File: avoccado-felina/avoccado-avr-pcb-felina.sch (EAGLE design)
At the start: 68 parts, among them Q1 16MHz, Q2 FET, U1 MPU-6000QFN-24, U2 MCP73831

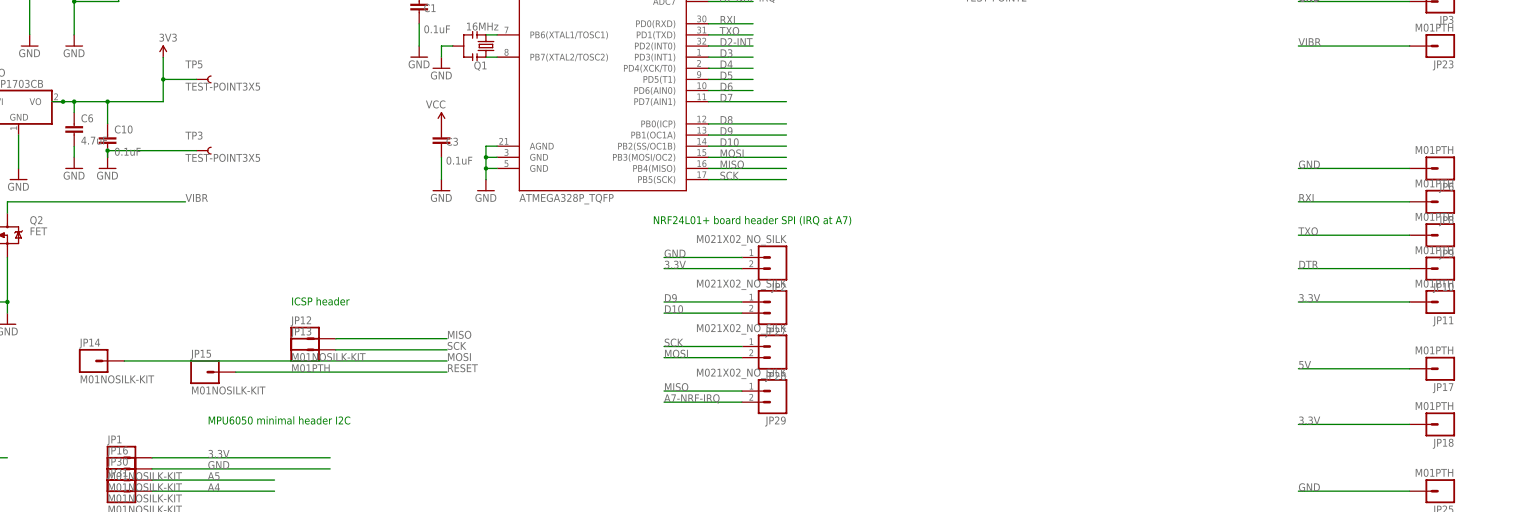
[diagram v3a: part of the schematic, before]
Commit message: Vcc and GND routed at bottom
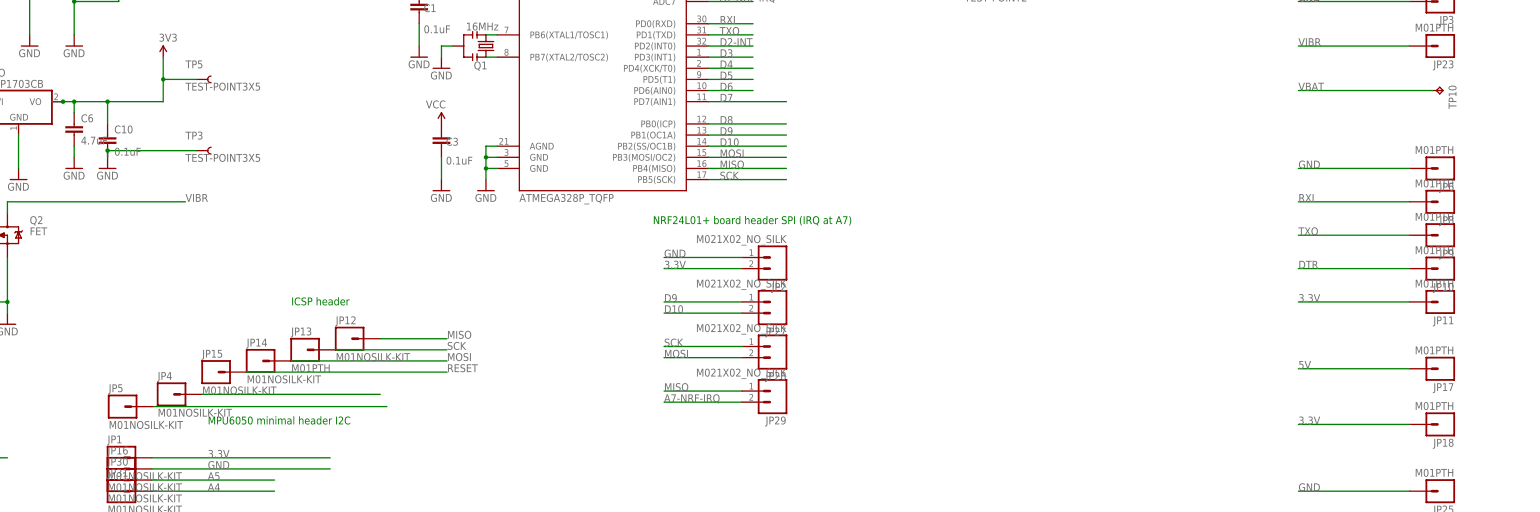
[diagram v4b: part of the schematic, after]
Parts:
- added JP4, JP5: M01NOSILK-KIT, SparkFun-Connectors:M01NOSILK-KIT
- added TP10: TPTP20R, testpad:TPTP20R
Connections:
- net 3.3V: now also JP4.1
- net GND: now also JP5.1
- net VBAT: now also TP10.TP
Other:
- moved on the sheet: JP12, JP14, JP15
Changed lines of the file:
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@@
 <part name="JP30" library="SparkFun-Connectors" deviceset="M01" device="NOSILK-KIT" value="M01NOSILK-KIT"/>
 <part name="JP31" library="SparkFun-Connectors" deviceset="M01" device="NOSILK-KIT" value="M01NOSILK-KIT"/>
+<part name="TP10" library="testpad" deviceset="TP" device="TP20R"/>
+<part name="JP4" library="SparkFun-Connectors" deviceset="M01" device="NOSILK-KIT" value="M01NOSILK-KIT"/>
+<part name="JP5" library="SparkFun-Connectors" deviceset="M01" device="NOSILK-KIT" value="M01NOSILK-KIT"/>
 </parts>
 <sheets>
@@
 <instance part="JP10" gate="G$1" x="383.54" y="76.2" rot="R180"/>
 <instance part="JP11" gate="G$1" x="383.54" y="68.58" rot="R180"/>
-<instance part="JP12" gate="G$1" x="123.19" y="60.198"/>
+<instance part="JP12" gate="G$1" x="133.35" y="60.198"/>
 <instance part="JP13" gate="G$1" x="123.19" y="57.658"/>
-<instance part="JP14" gate="G$1" x="74.93" y="55.118"/>
-<instance part="JP15" gate="G$1" x="100.33" y="52.578"/>
+<instance part="JP14" gate="G$1" x="113.03" y="55.118"/>
+<instance part="JP15" gate="G$1" x="102.87" y="52.578"/>
 <instance part="JP3" gate="G$1" x="383.54" y="137.16" rot="R180"/>
 <instance part="JP17" gate="G$1" x="383.54" y="53.34" rot="R180"/>
@@
 <instance part="JP30" gate="G$1" x="81.28" y="27.94"/>
 <instance part="JP31" gate="G$1" x="81.28" y="25.4"/>
+<instance part="TP10" gate="G$1" x="383.54" y="116.84" rot="R270"/>
+<instance part="JP4" gate="G$1" x="92.71" y="47.498"/>
+<instance part="JP5" gate="G$1" x="81.534" y="44.704"/>
 </instances>
 <busses>
@@
 <wire x1="-43.18" y1="121.92" x2="-43.18" y2="109.22" width="0.1524" layer="91"/>
 </segment>
+<segment>
+<wire x1="142.494" y1="44.704" x2="89.154" y2="44.704" width="0.1524" layer="91"/>
+<pinref part="JP5" gate="G$1" pin="1"/>
+</segment>
 </net>
 <net name="AREF" class="0">
@@
 </segment>
 <segment>
-<wire x1="156.21" y1="52.578" x2="107.95" y2="52.578" width="0.1524" layer="91"/>
+<wire x1="156.21" y1="52.578" x2="110.49" y2="52.578" width="0.1524" layer="91"/>
 <pinref part="JP15" gate="G$1" pin="1"/>
 <label x="156.21" y="52.578" size="1.778" layer="95"/>
@@
 </segment>
 <segment>
-<wire x1="156.21" y1="60.198" x2="130.81" y2="60.198" width="0.1524" layer="91"/>
+<wire x1="156.21" y1="60.198" x2="140.97" y2="60.198" width="0.1524" layer="91"/>
 <pinref part="JP12" gate="G$1" pin="1"/>
 <label x="156.21" y="60.198" size="1.778" layer="95"/>
@@
 </segment>
 <segment>
-<wire x1="156.21" y1="55.118" x2="82.55" y2="55.118" width="0.1524" layer="91"/>
+<wire x1="156.21" y1="55.118" x2="120.65" y2="55.118" width="0.1524" layer="91"/>
 <pinref part="JP14" gate="G$1" pin="1"/>
 <label x="156.21" y="55.118" size="1.778" layer="95"/>
@@
 <pinref part="P+4" gate="G$1" pin="3.3V"/>
 </segment>
+<segment>
+<wire x1="140.97" y1="47.498" x2="100.33" y2="47.498" width="0.1524" layer="91"/>
+<pinref part="JP4" gate="G$1" pin="1"/>
+</segment>
 </net>
 <net name="D9" class="0">
@@
 <pinref part="R8" gate="G$1" pin="2"/>
 </segment>
-</net>
+<segment>
+<wire x1="381" y1="116.84" x2="350.52" y2="116.84" width="0.1524" layer="91"/>
+<pinref part="TP10" gate="G$1" pin="TP"/>
+<label x="350.52" y="116.84" size="1.778" layer="95"/>
+</segment>
+</net>

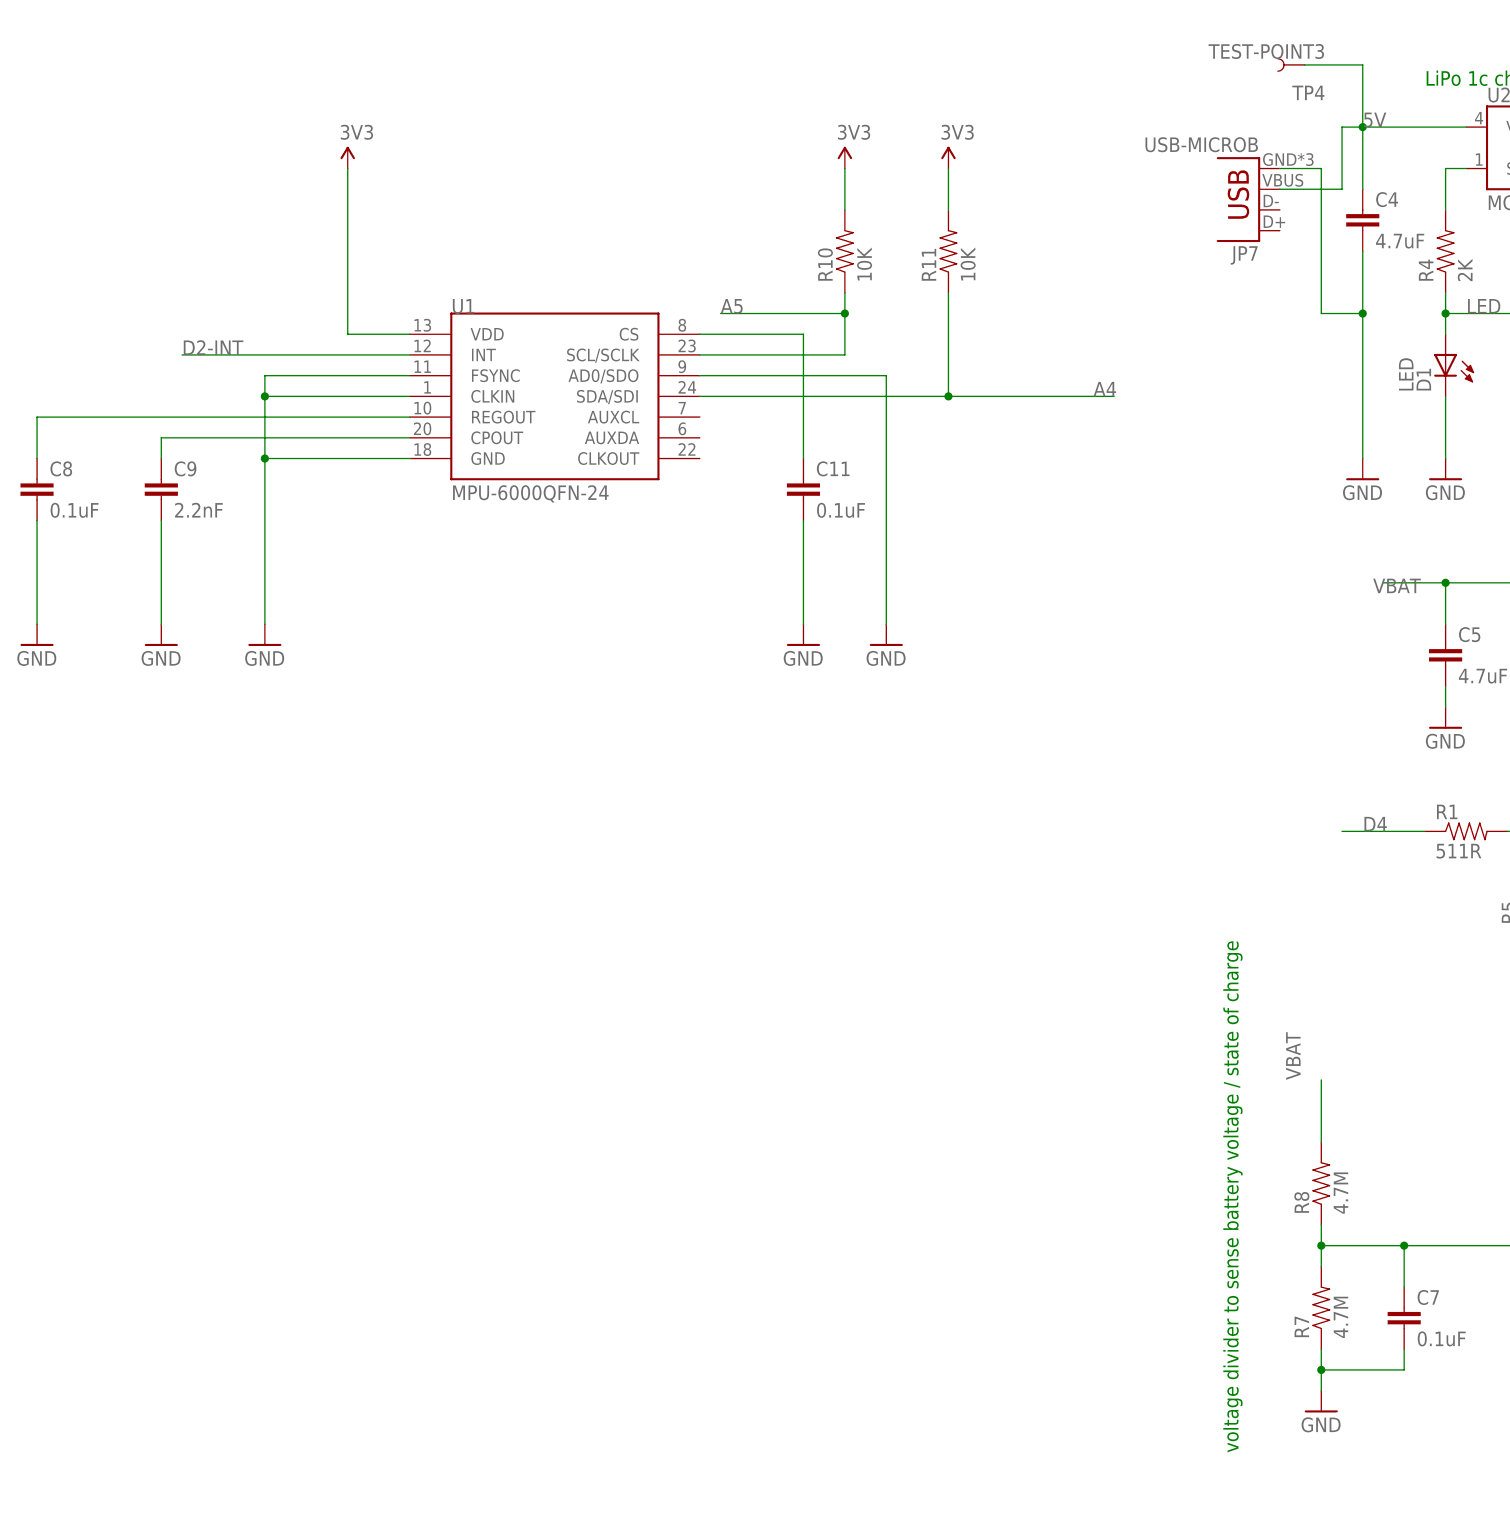
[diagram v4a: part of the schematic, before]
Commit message: route reset pullup
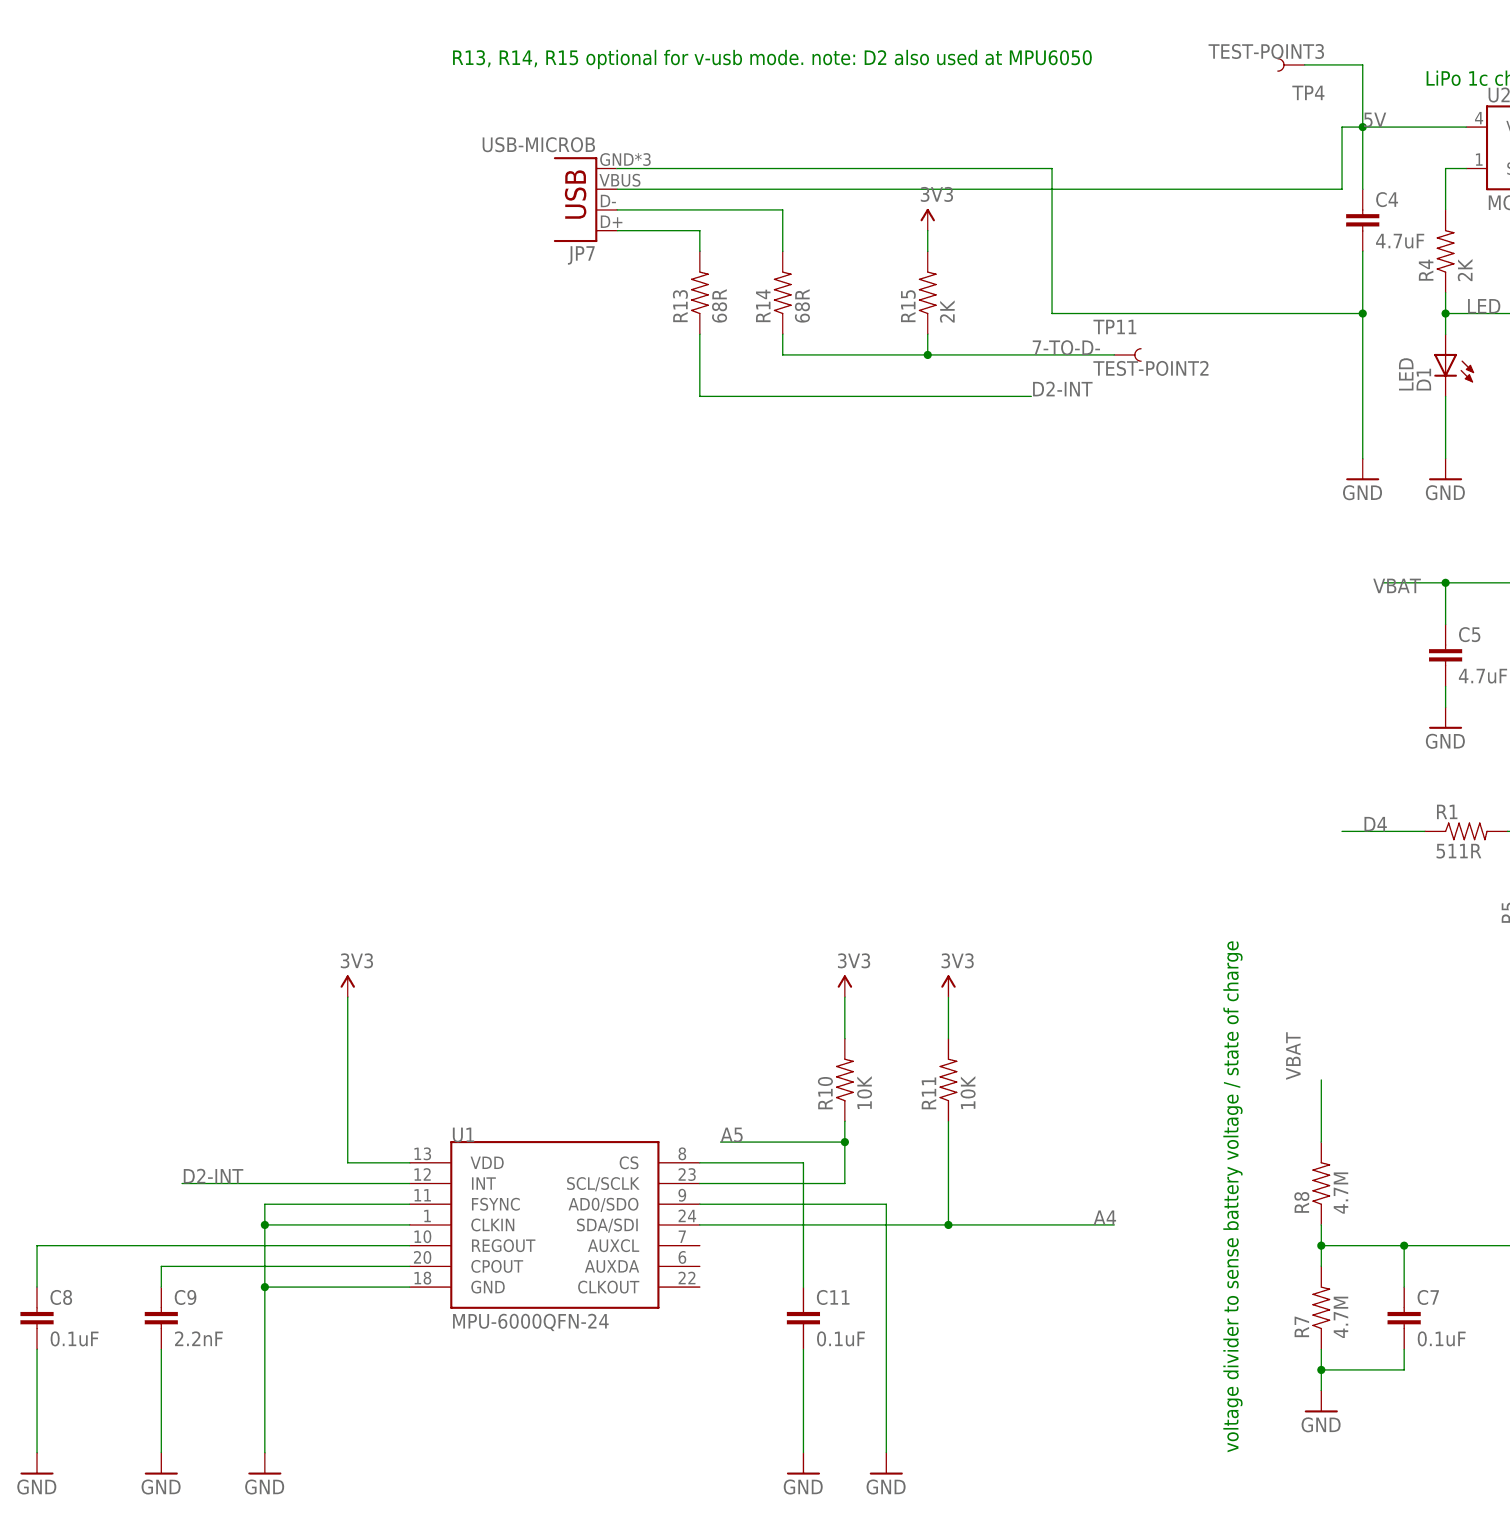
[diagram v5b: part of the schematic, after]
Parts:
- added R13, R14: 68R, SparkFun-Resistors:RESISTOR0603
- added R15: 2K, SparkFun-Resistors:RESISTOR0603
- added TP11: TEST-POINT2, SparkFun-Passives:TEST-POINT2
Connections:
- new net 7-TO-D-: R14.1, R15.1, TP11.1
- new net N$4: JP7.D+, R13.2
- new net N$5: JP7.D-, R14.2
- net 3.3V: now also R15.2
- net D2-INT: now also R13.1
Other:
- note added: "R13, R14, R15 optional for v-usb mode. note: D2 also used at MPU6050"
- moved on the sheet: C11, C8, C9, JP7, R10, R11, U1

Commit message: no airwires left :+1:  :shaved_ice:
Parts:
- removed JP22: M01NOSILK-KIT, SparkFun-Connectors:M01NOSILK-KIT
- removed JP26: M01PTH, SparkFun-Connectors:M01PTH
- added TP12, TP13, TP14: TPTP20R, testpad:TPTP20R
- TP4: value TEST-POINT3 -> TPTP20R; device SparkFun-Passives:TEST-POINT3 -> testpad:TPTP20R
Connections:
- net 3.3V: now also TP13.TP
- net 5V: now also TP14.TP; no longer TP4.1
- net A3: no longer JP22.1
- net GND: now also TP12.TP, TP4.TP; no longer JP26.1
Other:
- moved on the sheet: JP10, JP11, JP16, JP17, JP18, JP24, JP25, JP30, JP31, JP6, JP8, JP9

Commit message: cleanup schematics, add fiducials
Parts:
- added FID1, FID2, FID3, FID4: FIDUCIALUFIDUCIAL, SparkFun-Aesthetics:FIDUCIALUFIDUCIAL
- added LOGO1: OSHW-LOGOS, SparkFun-Aesthetics:OSHW-LOGOS
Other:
- note added: "Fiducials 1 mm round"
- note added: "MEMS"
- note added: "Needs to be bridged to D7 with an air wire for v-usb"
- note added: "Optional for v-usb"
- note added: "Power distribution"
- note added: "R3 determines the maximum charge current, 2K for 500 mA"
- note added: "TP and headers"
- note added: "main controller"
- note added: "misc"
- note added: "radio and MEMS connections"
- moved on the sheet: C10, C11, C4, C5, C6, C7, C8, C9, D1, JP1, JP10, JP11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
